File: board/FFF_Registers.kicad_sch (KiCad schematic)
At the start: 15 parts, among them U1 74F573, U14 74F32, U18 74F02, U2 74F541, U47 74F573, U48 74F541, U49 74F573, U50 74F541

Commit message: Board V1.1G
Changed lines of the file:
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@@
 (kicad_sch
-	(version 20231120)
+	(version 20250114)
 	(generator "eeschema")
-	(generator_version "8.0")
+	(generator_version "9.0")
 	(paper "USLetter")
 	(title_block
 		(title "FFFx Registers and Logic")
 		(date "2025-03-04")
-		(rev "1.0F")
+		(rev "1.1A")
 		(company "Data Tuning")
 		(comment 1 "Hydra 16")
@@
 	(label "T7"
 		(at 88.9 38.1 0)
-		(fields_autoplaced yes)
 		(effects
 			(font
@@
 	(label "T0"
 		(at 71.12 38.1 0)
-		(fields_autoplaced yes)
 		(effects
 			(font
@@
 	(label "D5"
 		(at 120.65 54.61 180)
-		(fields_autoplaced yes)
 		(effects
 			(font
@@
 	(label "D0"
 		(at 137.16 41.91 0)
-		(fields_autoplaced yes)
 		(effects
 			(font
@@
 	(label "D7"
 		(at 120.65 59.69 180)
-		(fields_autoplaced yes)
 		(effects
 			(font
@@
 	(label "D7"
 		(at 41.91 59.69 0)
-		(fields_autoplaced yes)
 		(effects
 			(font
@@
 	(label "T2"
 		(at 76.2 38.1 0)
-		(fields_autoplaced yes)
 		(effects
 			(font
@@
 	(label "D1"
 		(at 41.91 44.45 0)
-		(fields_autoplaced yes)
 		(effects
 			(font
@@
 	(label "U2"
 		(at 175.26 38.1 0)
-		(fields_autoplaced yes)
 		(effects
 			(font
@@
 	(label "D4"
 		(at 219.71 52.07 180)
-		(fields_autoplaced yes)
 		(effects
 			(font
@@
 	(label "D7"
 		(at 124.46 133.35 180)
-		(fields_autoplaced yes)
 		(effects
 			(font
@@
 	(label "V4"
 		(at 85.09 110.49 0)
-		(fields_autoplaced yes)
 		(effects
 			(font
@@
 	(label "D2"
 		(at 124.46 120.65 180)
-		(fields_autoplaced yes)
 		(effects
 			(font
@@
 	(label "D4"
 		(at 137.16 52.07 0)
-		(fields_autoplaced yes)
 		(effects
 			(font
@@
 	(label "T1"
 		(at 73.66 38.1 0)
-		(fields_autoplaced yes)
 		(effects
 			(font
@@
 	(label "V0"
 		(at 74.93 110.49 0)
-		(fields_autoplaced yes)
 		(effects
 			(font
@@
 	(label "U4"
 		(at 180.34 38.1 0)
-		(fields_autoplaced yes)
 		(effects
 			(font
@@
 	(label "V2"
 		(at 80.01 110.49 0)
-		(fields_autoplaced yes)
 		(effects
 			(font
@@
 	(label "D2"
 		(at 41.91 46.99 0)
-		(fields_autoplaced yes)
 		(effects
 			(font
@@
 	(label "D4"
 		(at 41.91 125.73 0)
-		(fields_autoplaced yes)
 		(effects
 			(font
@@
 	(label "D6"
 		(at 137.16 57.15 0)
-		(fields_autoplaced yes)
 		(effects
 			(font
@@
 	(label "D6"
 		(at 41.91 130.81 0)
-		(fields_autoplaced yes)
 		(effects
 			(font
@@
 	(label "D2"
 		(at 137.16 46.99 0)
-		(fields_autoplaced yes)
 		(effects
 			(font
@@
 	(label "V1"
 		(at 77.47 110.49 0)
-		(fields_autoplaced yes)
 		(effects
 			(font
@@
 	(label "U1"
 		(at 172.72 38.1 0)
-		(fields_autoplaced yes)
 		(effects
 			(font
@@
 	(label "T3"
 		(at 78.74 38.1 0)
-		(fields_autoplaced yes)
 		(effects
 			(font
@@
 	(label "D4"
 		(at 41.91 52.07 0)
-		(fields_autoplaced yes)
 		(effects
 			(font
@@
 	(label "U7"
 		(at 187.96 38.1 0)
-		(fields_autoplaced yes)
 		(effects
 			(font
@@
 	(label "D1"
 		(at 137.16 44.45 0)
-		(fields_autoplaced yes)
 		(effects
 			(font
@@
 	(label "U0"
 		(at 170.18 38.1 0)
-		(fields_autoplaced yes)
 		(effects
 			(font
@@
 	(label "D7"
 		(at 41.91 133.35 0)
-		(fields_autoplaced yes)
 		(effects
 			(font
@@
 	(label "D1"
 		(at 120.65 44.45 180)
-		(fields_autoplaced yes)
 		(effects
 			(font
@@
 	(label "D0"
 		(at 41.91 41.91 0)
-		(fields_autoplaced yes)
 		(effects
 			(font
@@
 	(label "D5"
 		(at 41.91 128.27 0)
-		(fields_autoplaced yes)
 		(effects
 			(font
@@
 	(label "U6"
 		(at 185.42 38.1 0)
-		(fields_autoplaced yes)
 		(effects
 			(font
@@
 	(label "D0"
 		(at 120.65 41.91 180)
-		(fields_autoplaced yes)
 		(effects
 			(font
@@
 	(label "D6"
 		(at 219.71 57.15 180)
-		(fields_autoplaced yes)
 		(effects
 			(font
@@
 	(label "D5"
 		(at 124.46 128.27 180)
-		(fields_autoplaced yes)
 		(effects
 			(font
@@
 	(label "D7"
 		(at 137.16 59.69 0)
-		(fields_autoplaced yes)
 		(effects
 			(font
@@
 	(label "V3"
 		(at 82.55 110.49 0)
-		(fields_autoplaced yes)
 		(effects
 			(font
@@
 	(label "D3"
 		(at 41.91 123.19 0)
-		(fields_autoplaced yes)
 		(effects
 			(font
@@
 	(label "V7"
 		(at 92.71 110.49 0)
-		(fields_autoplaced yes)
 		(effects
 			(font
@@
 	(label "D6"
 		(at 124.46 130.81 180)
-		(fields_autoplaced yes)
 		(effects
 			(font
@@
 	(label "D3"
 		(at 124.46 123.19 180)
-		(fields_autoplaced yes)
 		(effects
 			(font
@@
 	(label "D2"
 		(at 41.91 120.65 0)
-		(fields_autoplaced yes)
 		(effects
 			(font
@@
 	(label "D4"
 		(at 124.46 125.73 180)
-		(fields_autoplaced yes)
 		(effects
 			(font
@@
 	(label "D7"
 		(at 219.71 59.69 180)
-		(fields_autoplaced yes)
 		(effects
 			(font
@@
 	(label "D0"
 		(at 41.91 115.57 0)
-		(fields_autoplaced yes)
 		(effects
 			(font
@@
 	(label "D6"
 		(at 120.65 57.15 180)
-		(fields_autoplaced yes)
 		(effects
 			(font
@@
 	(label "T6"
 		(at 86.36 38.1 0)
-		(fields_autoplaced yes)
 		(effects
 			(font
@@
 	(label "T5"
 		(at 83.82 38.1 0)
-		(fields_autoplaced yes)
 		(effects
 			(font
@@
 	(label "D2"
 		(at 120.65 46.99 180)
-		(fields_autoplaced yes)
 		(effects
 			(font
@@
 	(label "D3"
 		(at 137.16 49.53 0)
-		(fields_autoplaced yes)
 		(effects
 			(font
@@
 	(label "D5"
 		(at 41.91 54.61 0)
-		(fields_autoplaced yes)
 		(effects
 			(font
@@
 	(label "D3"
 		(at 219.71 49.53 180)
-		(fields_autoplaced yes)
 		(effects
 			(font
@@
 	(label "V5"
 		(at 87.63 110.49 0)
-		(fields_autoplaced yes)
 		(effects
 			(font
@@
 	(label "D3"
 		(at 41.91 49.53 0)
-		(fields_autoplaced yes)
 		(effects
 			(font
@@
 	(label "D6"
 		(at 41.91 57.15 0)
-		(fields_autoplaced yes)
 		(effects
 			(font
@@
 	(label "V6"
 		(at 90.17 110.49 0)
-		(fields_autoplaced yes)
 		(effects
 			(font
@@
 	(label "D2"
 		(at 219.71 46.99 180)
-		(fields_autoplaced yes)
 		(effects
 			(font
@@
 	(label "D1"
 		(at 124.46 118.11 180)
-		(fields_autoplaced yes)
 		(effects
 			(font
@@
 	(label "D4"
 		(at 120.65 52.07 180)
-		(fields_autoplaced yes)
 		(effects
 			(font
@@
 	(label "U3"
 		(at 177.8 38.1 0)
-		(fields_autoplaced yes)
 		(effects
 			(font
@@
 	(label "T4"
 		(at 81.28 38.1 0)
-		(fields_autoplaced yes)
 		(effects
 			(font
@@
 	(label "D5"
 		(at 219.71 54.61 180)
-		(fields_autoplaced yes)
 		(effects
 			(font
@@
 	(label "D0"
 		(at 124.46 115.57 180)
-		(fields_autoplaced yes)
 		(effects
 			(font
@@
 	(label "D1"
 		(at 219.71 44.45 180)
-		(fields_autoplaced yes)
 		(effects
 			(font
@@
 	(label "U5"
 		(at 182.88 38.1 0)
-		(fields_autoplaced yes)
 		(effects
 			(font
@@
 	(label "D5"
 		(at 137.16 54.61 0)
-		(fields_autoplaced yes)
 		(effects
 			(font
@@
 	(label "D1"
 		(at 41.91 118.11 0)
-		(fields_autoplaced yes)
 		(effects
 			(font
@@
 	(label "D3"
 		(at 120.65 49.53 180)
-		(fields_autoplaced yes)
 		(effects
 			(font
@@
 	(label "D0"
 		(at 219.71 41.91 180)
-		(fields_autoplaced yes)
 		(effects
 			(font

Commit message: V1.3 Initial (preliminary) checkin
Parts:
- removed U14: 74F32, Package_DIP:DIP-14_W7.62mm_Socket_LongPads, symbol 74xx:74LS32
- removed unit 1 of U18
- removed unit 3 of U18
- removed unit 2 of U18
- added C76, C77: 104, Capacitor_THT:C_Disc_D5.0mm_W2.5mm_P5.00mm, symbol Device:C_Small
- added U58: 74F573, Package_DIP:DIP-20_W7.62mm_Socket_LongPads, symbol 74xx:74LS573
- added U59: 74F541, Package_DIP:DIP-20_W7.62mm_Socket_LongPads, symbol 74xx:74LS541
- added U60: GAL16V8, Package_DIP:DIP-20_W7.62mm_Socket_LongPads, symbol Logic_Programmable:GAL16V8
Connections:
- net !RWB: now also U59.1 (G1)
- net +5V: now also U60.20 (VCC)
- net D0: now also U58.2 (D0), U59.18 (Y0)
- net D1: now also U58.3 (D1), U59.17 (Y1)
- net D2: now also U58.4 (D2), U59.16 (Y2)
- net D3: now also U58.5 (D3), U59.15 (Y3)
- net D4: now also U58.6 (D4), U59.14 (Y4)
- net D5: now also U58.7 (D5), U59.13 (Y5)
- net D6: now also U58.8 (D6), U59.12 (Y6)
- net D7: now also U58.9 (D7), U59.11 (Y7)
- net FFF0_L: now also U60.18 (IO2)
- net FFF1_L: now also U60.16 (IO4)
- net FFF2_L: now also U60.14 (IO6)
- net GND: now also C76.2, C77.1, U58.1 (OE), U58.10 (GND), U59.10 (GND), U60.10 (GND)
- net nFFF0_S: now also U60.19 (IO1)
- net nFFF1_S: now also U60.17 (I03)
- net nFFF2_S: now also U60.15 (IO5)
- net nIOB0_S: now also U60.3 (I3)
- net nIOB1_S: now also U60.4 (I4)
- net nIOB2_S: now also U60.5 (I5)
- net nIOP15_S: now also U60.2 (I2)
- new net: C76.1, U58.20 (VCC)
- new net: C77.2, U59.20 (VCC)
- new net FFF3_L: U58.11 (Load), U60.12 (IO8)
- new net P_RWB: U60.9 (I9)
- new net W0: U58.19 (Q0), U59.2 (A0)
- new net W1: U58.18 (Q1), U59.3 (A1)
- new net W2: U58.17 (Q2), U59.4 (A2)
- new net W3: U58.16 (Q3), U59.5 (A3)
- new net W4: U58.15 (Q4), U59.6 (A4)
- new net W5: U58.14 (Q5), U59.7 (A5)
- new net W6: U58.13 (Q6), U59.8 (A6)
- new net W7: U58.12 (Q7), U59.9 (A7)
- new net nFFF3_S: U59.19 (G2), U60.13 (IO7)
- new net nIOB3_S: U60.6 (I6)
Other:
- moved on the sheet: C63, C64, U49, U50

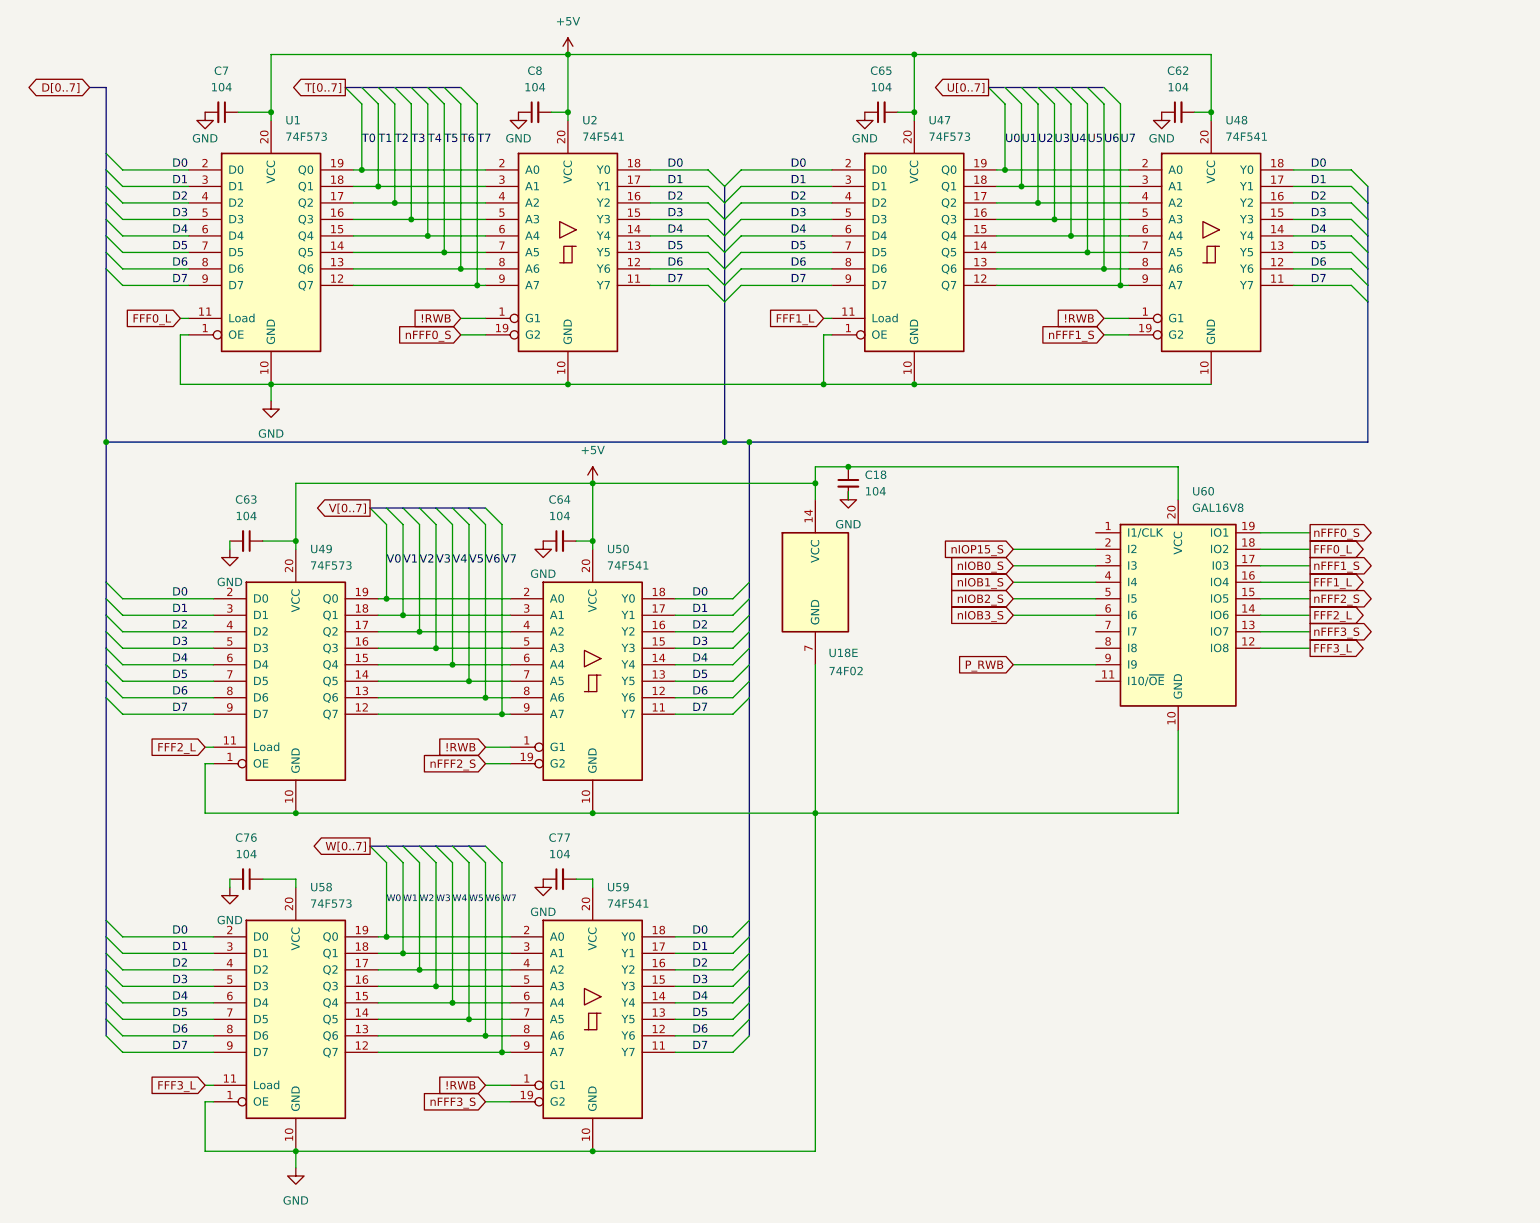
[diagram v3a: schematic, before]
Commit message: V1.3C without board traces
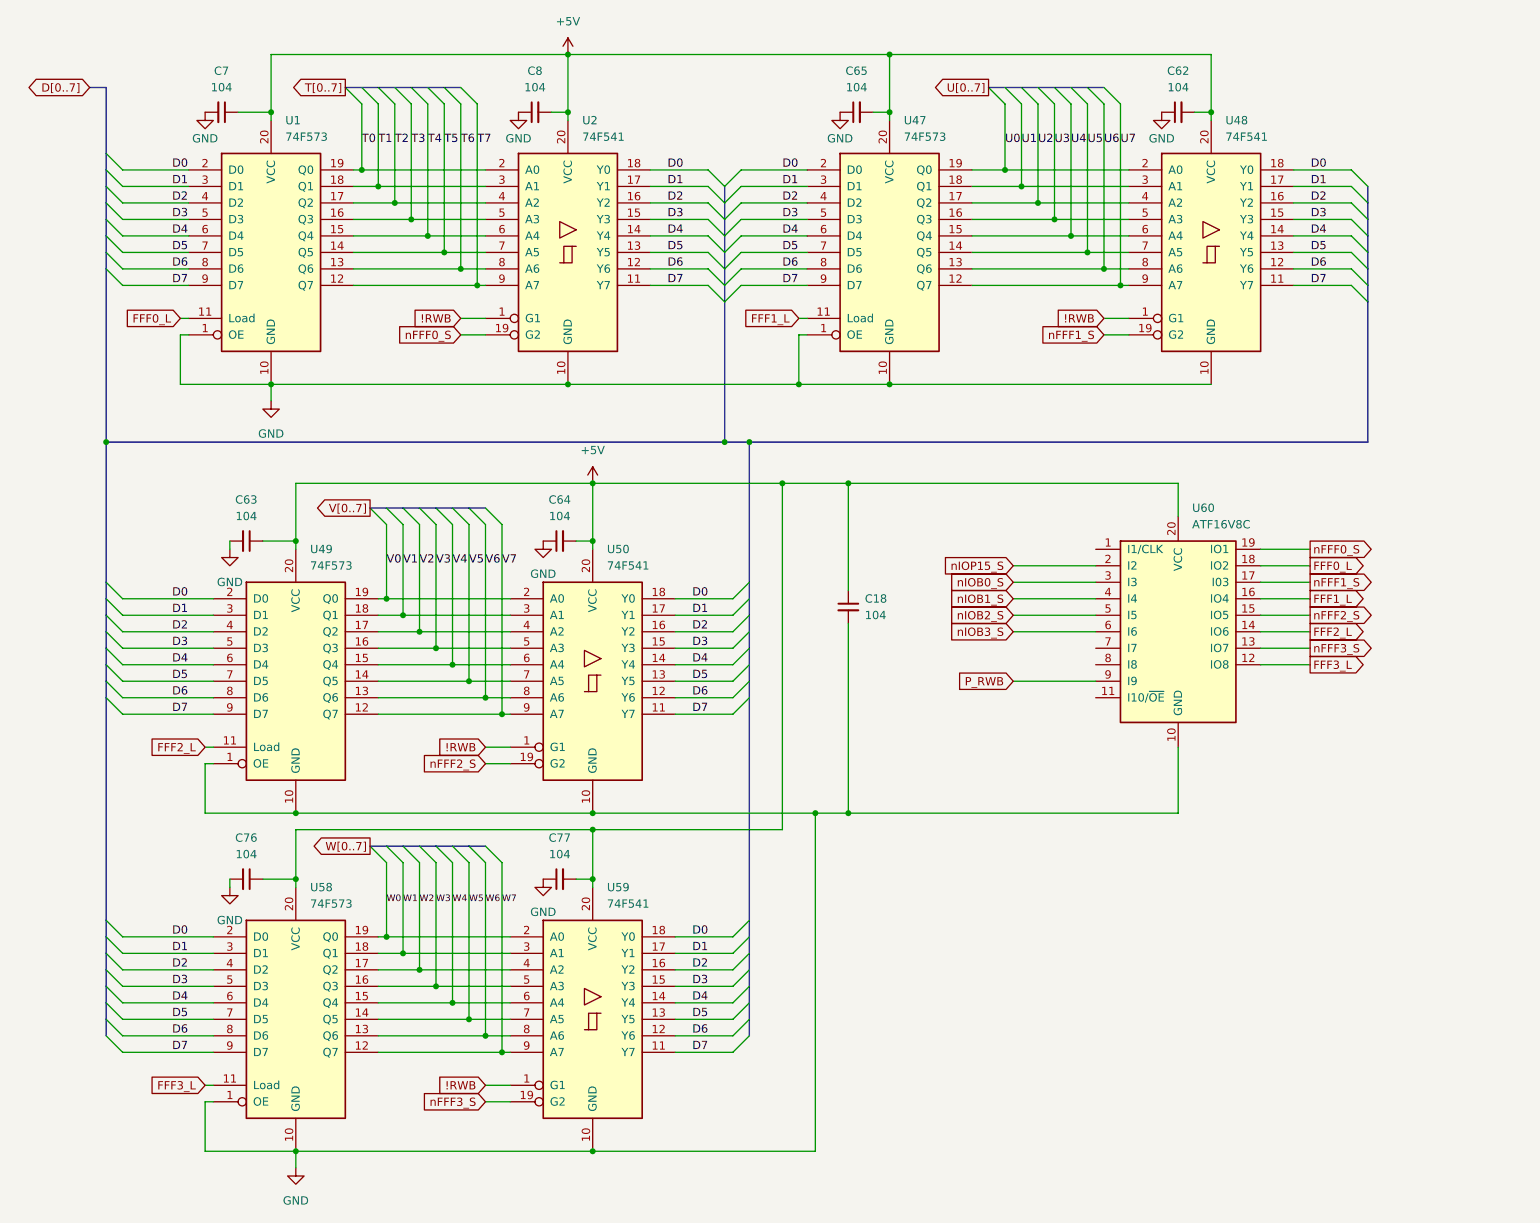
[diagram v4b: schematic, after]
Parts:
- removed U18: 74F02, Package_DIP:DIP-14_W7.62mm_Socket_LongPads, symbol 74xx:7402
- U60: value GAL16V8 -> ATF16V8C
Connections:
- net +5V: now also C76.1, C77.2, U58.20 (VCC), U59.20 (VCC)
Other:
- moved on the sheet: C18, C65, U47, U60

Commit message: Version 1.7A: More rearrangement, partial wiring of PDB, addition of W register
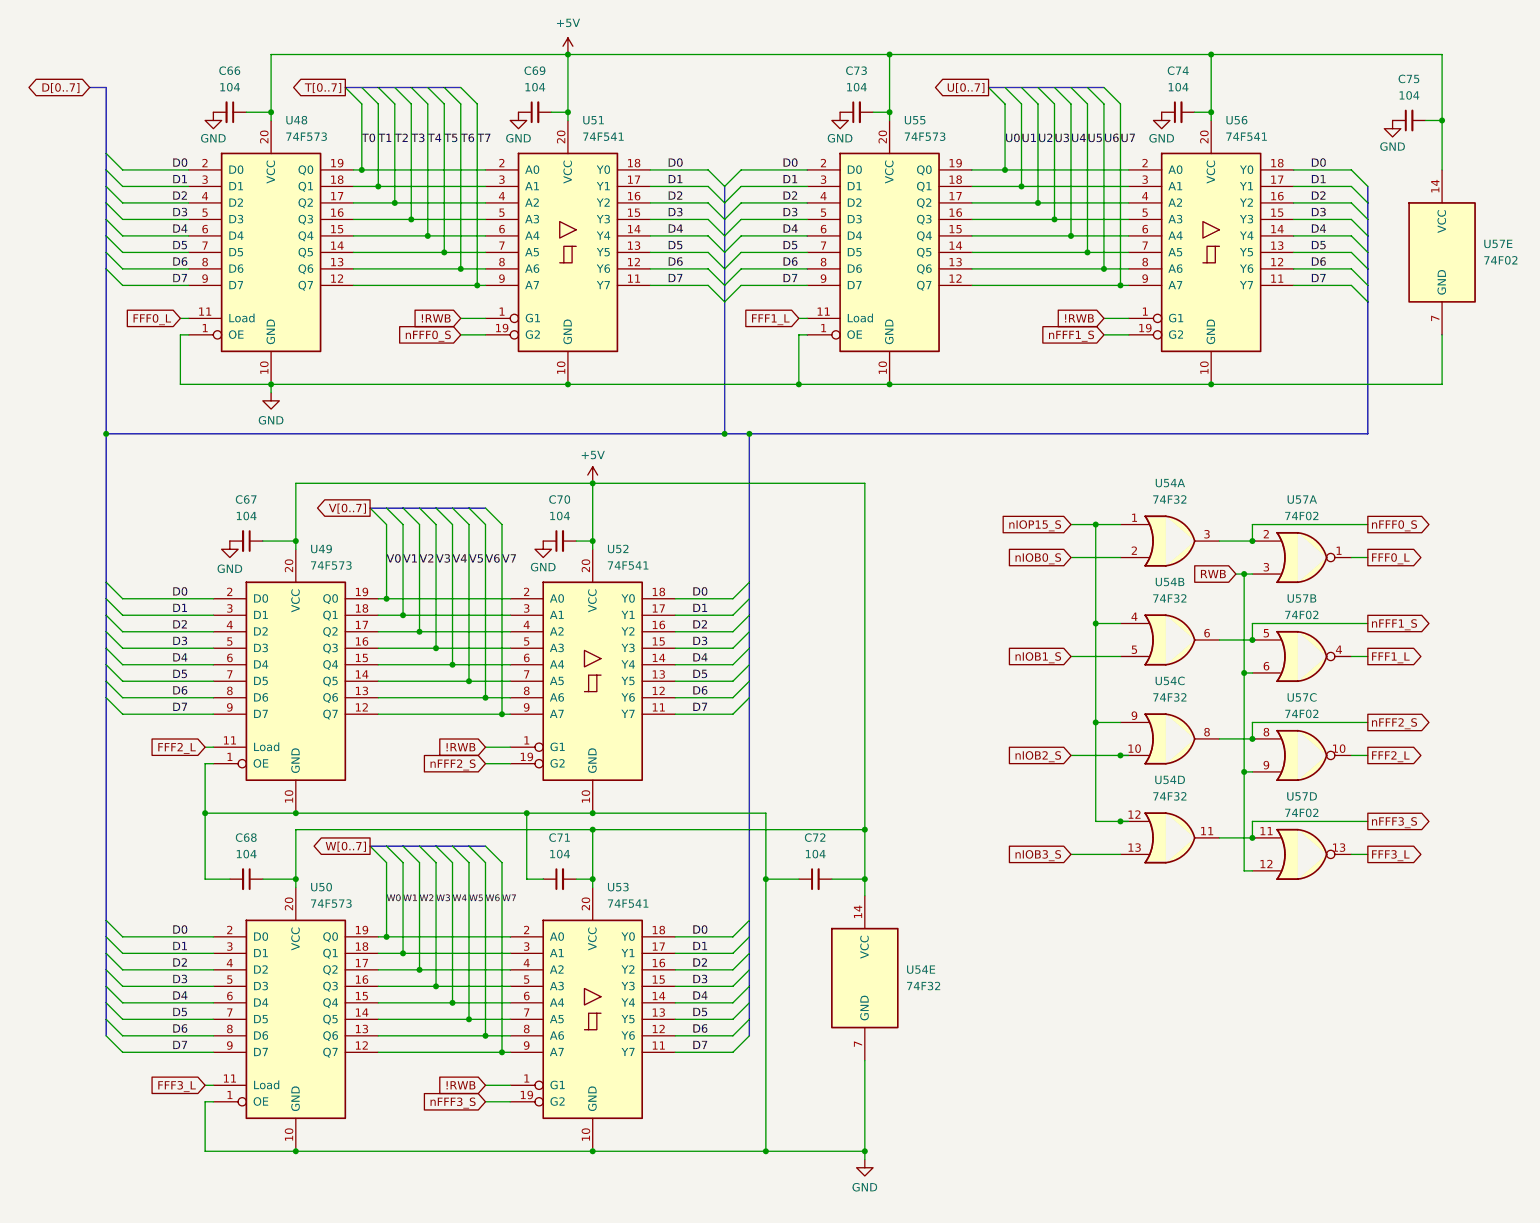
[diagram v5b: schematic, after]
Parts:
- removed U60: ATF16V8C, Package_DIP:DIP-20_W7.62mm_Socket_LongPads, symbol Logic_Programmable:GAL16V8
- added C75: 104, Capacitor_THT:C_Disc_D5.0mm_W2.5mm_P5.00mm, symbol Device:C_Small
- added U54: 74F32, Package_DIP:DIP-14_W7.62mm_Socket_LongPads, symbol 74xx:74LS32
- added U57: 74F02, Package_DIP:DIP-14_W7.62mm_Socket_LongPads, symbol 74xx:74LS02
- renumbered C7 to C66, C63 to C67, C76 to C68, C8 to C69, C64 to C70, C77 to C71, C18 to C72, C65 to C73, C62 to C74, U1 to U48, U58 to U50, U2 to U51, U50 to U52, U59 to U53, U47 to U55, U48 to U56
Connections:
- net +5V: now also C72.2, C75.2, U54.14 (VCC), U57.14 (VCC); no longer C72.1
- net FFF0_L: now also U57.1
- net FFF1_L: now also U57.4
- net FFF2_L: now also U57.10
- net FFF3_L: now also U57.13
- net GND: now also C72.1, C75.1, U54.7 (GND), U57.7 (GND); no longer C72.2
- net nFFF0_S: now also U54.3, U57.2
- net nFFF1_S: now also U54.6, U57.5
- net nFFF2_S: now also U54.8, U57.8
- net nFFF3_S: now also U54.11, U57.11
- net nIOB0_S: now also U54.2
- net nIOB1_S: now also U54.5
- net nIOB2_S: now also U54.10
- net nIOB3_S: now also U54.13
- net nIOP15_S: now also U54.1, U54.12, U54.4, U54.9
- new net RWB: U57.12, U57.3, U57.6, U57.9
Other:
- moved on the sheet: C66, C72
